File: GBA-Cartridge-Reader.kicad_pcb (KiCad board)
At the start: 2 copper layers, 5 parts, among them U1 ATmega32U4-A

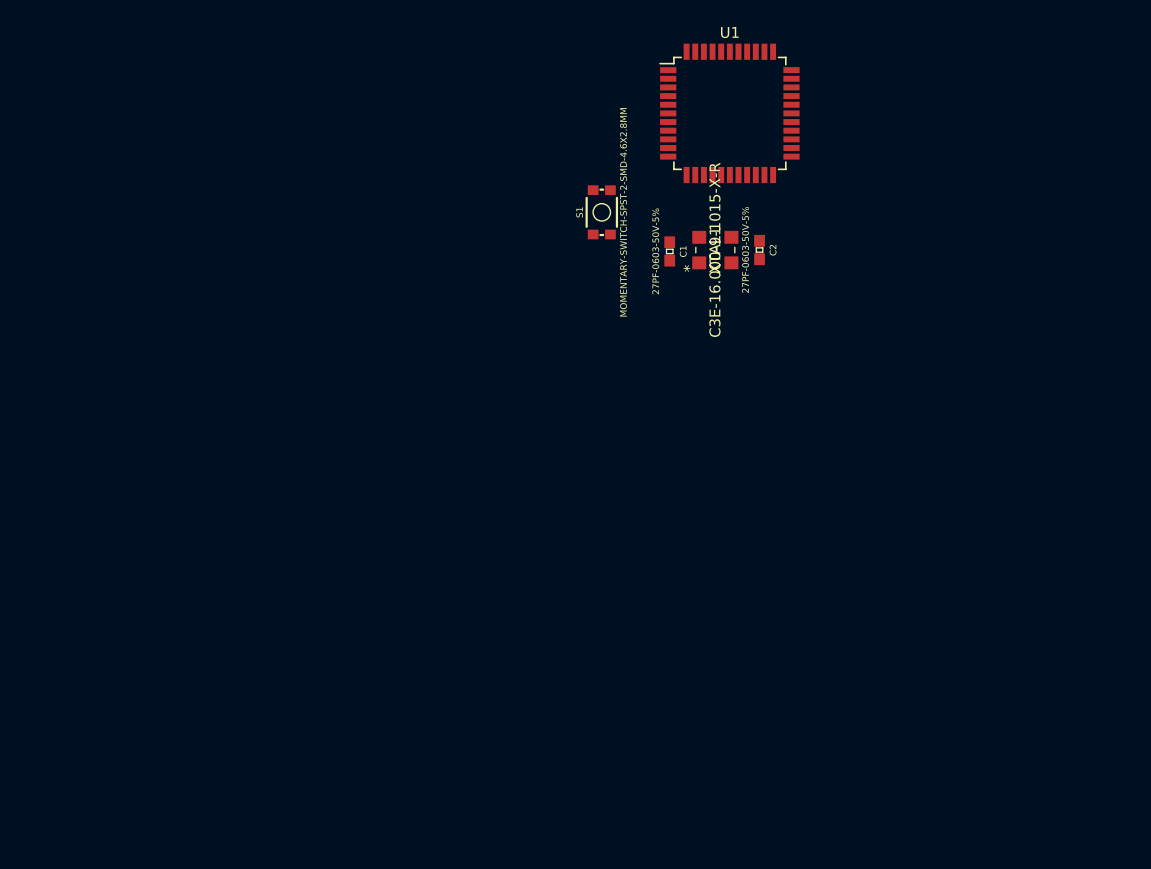
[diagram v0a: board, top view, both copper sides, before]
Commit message: Micro population complete.
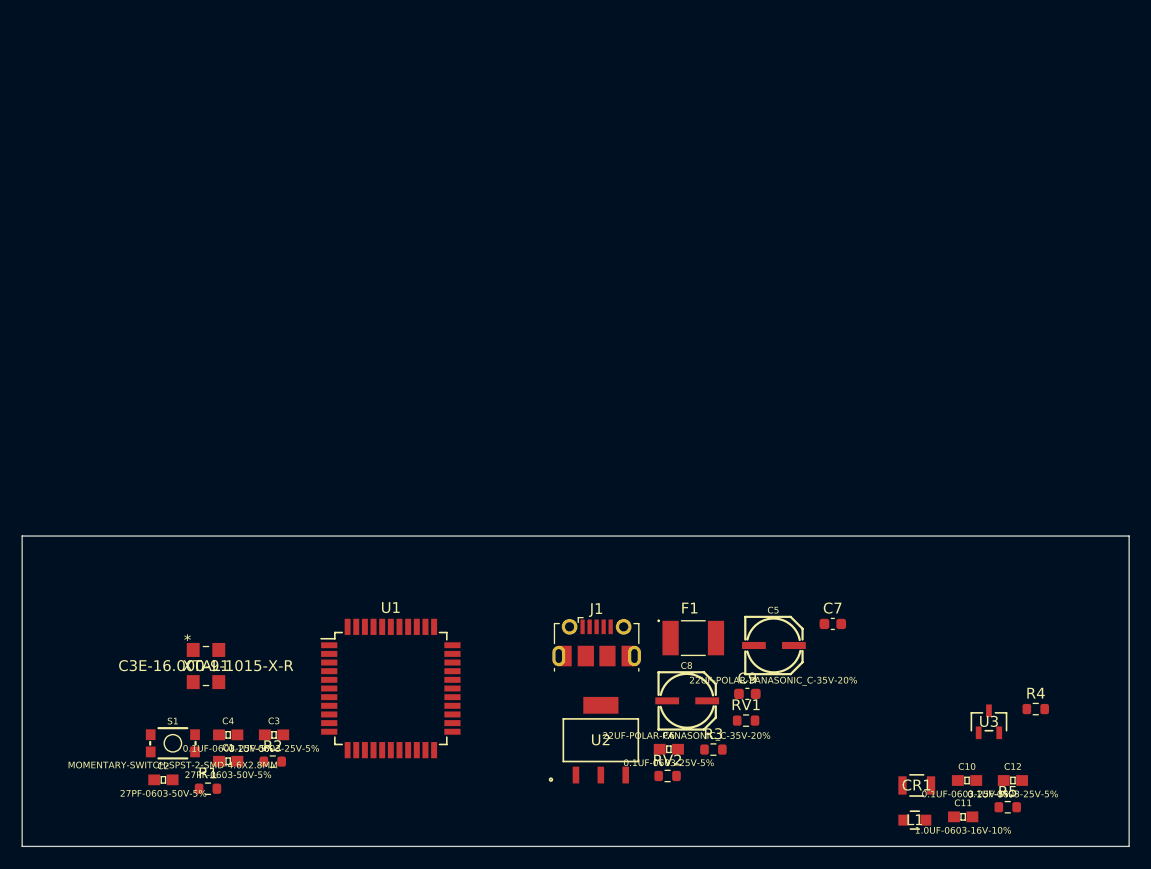
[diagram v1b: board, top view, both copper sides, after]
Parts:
- added C10: 0.1UF-0603-25V-5%, Sparkfun-Capacitors:0603, F.Cu at (224.5, 118.6)
- added C11: 1.0UF-0603-16V-10%, Sparkfun-Capacitors:0603, F.Cu at (224.2, 122.0)
- added C12: 0.1UF-0603-25V-5%, Sparkfun-Capacitors:0603, F.Cu at (228.8, 118.6)
- added C3: 0.1UF-0603-25V-5%, Sparkfun-Capacitors:0603, F.Cu at (160.4, 114.4)
- added C4: 0.1UF-0603-25V-5%, Sparkfun-Capacitors:0603, F.Cu at (156.2, 114.4)
- added C5: 22UF-POLAR-PANASONIC_C-35V-20%, Sparkfun-Capacitors:PANASONIC_C, F.Cu at (206.6, 105.9)
- added C6: 0.1UF-0603-25V-5%, Sparkfun-Capacitors:0603, F.Cu at (197.0, 115.7)
- added C7: 0.1UF-0603-25V-5%, Capacitor_SMD:C_0603_1608Metric, F.Cu at (212.1, 104.1)
- added C8: 22UF-POLAR-PANASONIC_C-35V-20%, Sparkfun-Capacitors:PANASONIC_C, F.Cu at (198.6, 111.1)
- added C9: 0.1UF-0603-25V-5%, Capacitor_SMD:C_0603_1608Metric, F.Cu at (204.2, 110.6)
- added CR1: CD1206-S01575, Arduino Diode:DIODE_CD1206-S01575_BRN, F.Cu at (219.9, 119.1)
- added F1: MF-MSMF050-2, USB Fuse:FUSM4632X85, F.Cu at (199.2, 105.4)
- added J1: USB_B_Micro, Connector_USB:USB_Micro-B_Molex-105017-0001, F.Cu at (190.3, 105.9)
- added L1: MH2029-300Y, Arduino Buck:IND_BOURNS_MH2029, F.Cu at (219.7, 122.3)
- added R1: 22R, Resistor_SMD:R_0603_1608Metric, F.Cu at (154.3, 119.4)
- added R2: 22R, Resistor_SMD:R_0603_1608Metric, F.Cu at (160.3, 116.9)
- added R3: 10K, Resistor_SMD:R_0603_1608Metric, F.Cu at (201.1, 115.8)
- added R4: 10K, Resistor_SMD:R_0603_1608Metric, F.Cu at (230.9, 112.0)
- added R5: 10K, Resistor_SMD:R_0603_1608Metric, F.Cu at (228.3, 121.1)
- added RV1: Varistor_US, Resistor_SMD:R_0603_1608Metric, F.Cu at (204.1, 113.1)
- added RV2: Varistor_US, Resistor_SMD:R_0603_1608Metric, F.Cu at (196.8, 118.2)
- added U2: NCP1117ST50T3, 5V Regulator:SOT223-3_ONS, F.Cu at (190.7, 114.9)
- added U3: PMV48XP_215, USB MOSFET:TO-236_SOT23_NEX, F.Cu at (226.6, 113.2)
- moved C2 73.8 mm to (150.2, 118.6), turned to 0 degrees
- moved S1 63.1 mm to (151.1, 115.2), turned to 0 degrees
- moved C1 62.4 mm to (156.2, 116.8), turned to 0 degrees
- moved U1 61.7 mm to (171.3, 110.1)
- moved XTAL1 60.8 mm to (154.2, 108.0), turned to 0 degrees
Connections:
- U1 pad 14: Net-(U1-Pad14) -> +5V
- U1 pad 15: Net-(U1-Pad15) -> GND
- U1 pad 2: unconnected-(U1-Pad2) -> +5V
- U1 pad 23: Net-(U1-Pad15) -> GND
- U1 pad 3: unconnected-(U1-Pad3) -> Net-(R1-Pad1)
- U1 pad 34: Net-(U1-Pad14) -> +5V
- U1 pad 35: Net-(U1-Pad15) -> GND
- U1 pad 4: unconnected-(U1-Pad4) -> Net-(R2-Pad2)
- U1 pad 42: unconnected-(U1-Pad42) -> Net-(U1-Pad42)
- U1 pad 43: Net-(U1-Pad15) -> GND
- U1 pad 5: unconnected-(U1-Pad5) -> GND
- U1 pad 6: unconnected-(U1-Pad6) -> Net-(U1-Pad6)
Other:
- board outline added: 102.4 x 28.7 mm
